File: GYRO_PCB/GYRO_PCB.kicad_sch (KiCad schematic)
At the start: 0 parts

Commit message: feat: add symbols and footprints for principal components
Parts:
- added J1: Pmod GYRO, Connector_PinSocket_2.54mm:PinSocket_2x04_P2.54mm_Vertical, symbol Connector_Generic:Conn_02x04_Counter_Clockwise
- added J2: FLASH Socket 1, Connector_PinSocket_2.54mm:PinSocket_1x08_P2.54mm_Vertical, symbol Connector:Conn_01x08_Socket
- added J3: FLASH Socket 2, Connector_PinSocket_2.54mm:PinSocket_1x08_P2.54mm_Vertical, symbol Connector:Conn_01x08_Socket
- added U1: NUCLEO-F446RE, FOOTPRINTS:NUCLEO-F446RE, symbol NUCLEO-F446RE:NUCLEO-F446RE
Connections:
- new net: U1.CN7_19 (CN7_GND), U1.CN7_20 (CN7_GND), U1.CN7_22 (CN7_GND), U1.CN7_8 (CN7_GND)

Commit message: feat: most of schematic done
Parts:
- removed U1: NUCLEO-F446RE, FOOTPRINTS:NUCLEO-F446RE, symbol NUCLEO-F446RE:NUCLEO-F446RE
- added C1: 0.1uF, symbol Device:C
- added R1, R2, R3: 100k, symbol Device:R
- added R4, R5, R6, R7: 10k, symbol Device:R
- added U1: NUCLEO64-F446RE, FOOTPRINTS:NUCLEO-F446RE, symbol NUCLEO-F446RE:NUCLEO64-F411RE
- J1: footprint Connector_PinSocket_2.54mm:PinSocket_2x04_P2.54mm_Vertical -> GYRO:PinSocket_2x04_P2.54mm_Vertical_Custom
- J3: footprint Connector_PinSocket_2.54mm:PinSocket_1x08_P2.54mm_Vertical -> GYRO:PinSocket_1x08_P2.54mm_Vertical_Custom
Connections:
- net GND: now reaches J3.10 (VSS)
- net GND: now also J1.7 (GND), C1.2
- net NUCLEO_FLASH_SPI2_MOSI: now reaches J3.15 (DQ0)
- net NUCLEO_FLASH_SPI2_MOSI: now also R7.2, U1.CN10_26 (PB15)
- net NUCLEO_FLASH_SCLK: now reaches J3.16 (C)
- net NUCLEO_FLASH_SCLK: now also R6.2, U1.CN5_2 (PC7)
- net at J3.9 (W#/DQ2): now also R3.1
- net at J2.1 (DQ3/HOLD#): now also R1.2
- net +3V3: now reaches J2.2 (VCC)
- net +3V3: now also J1.8 (VCC), C1.1, R1.1, R2.1, R3.2, R4.2, R5.2, R6.1, R7.1
- net at J2.3 (RESET#): now also R2.2
- net NUCLEO_FLASH_CS: now reaches J2.7 (S#)
- net NUCLEO_FLASH_CS: now also R4.1, U1.CN8_3 (PA4)
- net NUCLEO_FLASH_SPI2_MISO: now reaches J2.8 (DQ1)
- net NUCLEO_FLASH_SPI2_MISO: now also R5.1, U1.CN10_28 (PB14)
- net NUCLEO_GYRO_I2C1_SCL: now reaches J1.5 (SCL)
- net NUCLEO_GYRO_I2C1_SCL: now also U1.CN5_10 (PB8)
- net NUCLEO_GYRO_I2C1_SDA: now reaches J1.6 (SDA)
- net NUCLEO_GYRO_I2C1_SDA: now also U1.CN5_9 (PB9)
- no-connect marks 0 -> 11

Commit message: feat: finish PCB draft
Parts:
- added H1, H2, H3, H4: MountingHole, MountingHole:MountingHole_2.2mm_M2_ISO14580, symbol Mechanical:MountingHole
- added J4: Power Terminal, TerminalBlock_MetzConnect:TerminalBlock_MetzConnect_Type011_RT05503HBLC_1x03_P5.00mm_Horizontal, symbol Connector:Screw_Terminal_01x03
- C1: footprint (none) -> Capacitor_THT:C_Disc_D8.0mm_W2.5mm_P5.00mm
- R1, R2, R3, R4, R5, R6, R7: footprint (none) -> Resistor_THT:R_Axial_DIN0207_L6.3mm_D2.5mm_P10.16mm_Horizontal
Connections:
- net +3V3: now also J4.1 (Pin_1)
- net GND: now also U1.CN6_6 (GND), U1.CN6_7 (GND), J4.3 (Pin_3)
- new net NUCLEO_E5V: J4.2 (Pin_2), U1.CN7_6 (E5V)
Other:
- note added: "IMPORTANT: E5V is the external power supply If this order is not respected, the board / PC might be damaged 1. Connect the jumper between pin 2 and pin 3 of JP5 2. Check that JP1 is removed 3. Connect the external power source to E5V (CN7 pin 6) - Already handled by the PCB Use the Power Terminal 4. Power on the external power supply (5 V) 5. Check that LD3 is turned ON 6. Connect the PC to USB c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"
- moved on the sheet: C1, J1, J2, J3, R1, R2, R3, R4, R5, R6, R7

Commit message: Add files via upload
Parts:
- removed J4: Power Terminal, TerminalBlock_MetzConnect:TerminalBlock_MetzConnect_Type011_RT05503HBLC_1x03_P5.00mm_Horizontal, symbol Connector:Screw_Terminal_01x03
- added C2: 0.33uF, Capacitor_THT:C_Disc_D8.0mm_W2.5mm_P5.00mm, symbol Device:C
- added C3: 0.1uF, Capacitor_THT:C_Disc_D8.0mm_W2.5mm_P5.00mm, symbol Device:C
- added J5: Power Terminal - Raw, symbol Connector:Screw_Terminal_01x02
- added U2: uA7805, symbol Regulator_Linear:uA7805
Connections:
- net +3V3: now also U1. (PB13)
- net GND: now also C2.1, C3.1, J5.2 (Pin_2), U2.2 (GND)
- net NUCLEO_E5V: now also C3.2, U2.3 (OUT)
- new net BAT: C2.2, J5.1 (Pin_1), U2.1 (IN)
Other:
- note added: "IMPORTANT: E5V is the external power supply If this order is not respected, the board / PC might be damaged 1. Connect the jumper between pin 2 and pin 3 of JP5 2. Check that JP1 is removed 3. Connect the external power source to E5V (CN7 pin 6) - Already handled by the PCB Use the Power Terminal 4. Power on the external power supply () 5. Check that LD3 is turned ON 6. Connect the PC to USB conn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"
- note removed: "IMPORTANT: E5V is the external power supply If this order is not respected, the board / PC might be damaged 1. Connect the jumper between pin 2 and pin 3 of JP5 2. Check that JP1 is removed 3. Connect the external power source to E5V (CN7 pin 6) - Already handled by the PCB Use the Power Terminal 4. Power on the external power supply (5 V) 5. Check that LD3 is turned ON 6. Connect the PC to USB c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"

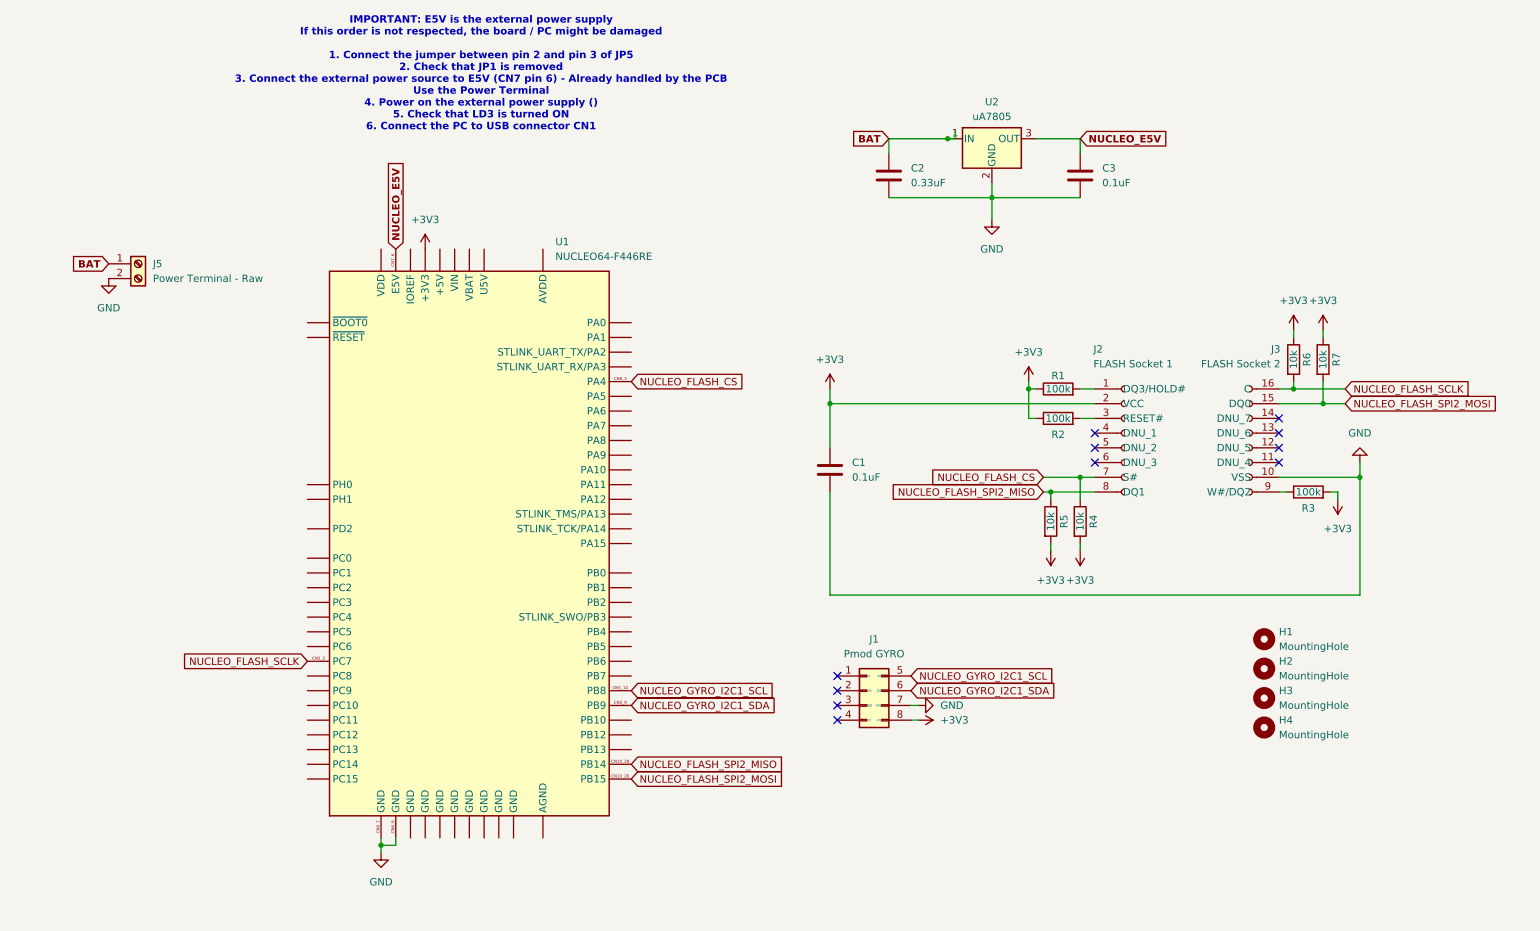
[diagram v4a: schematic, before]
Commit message: New schematic
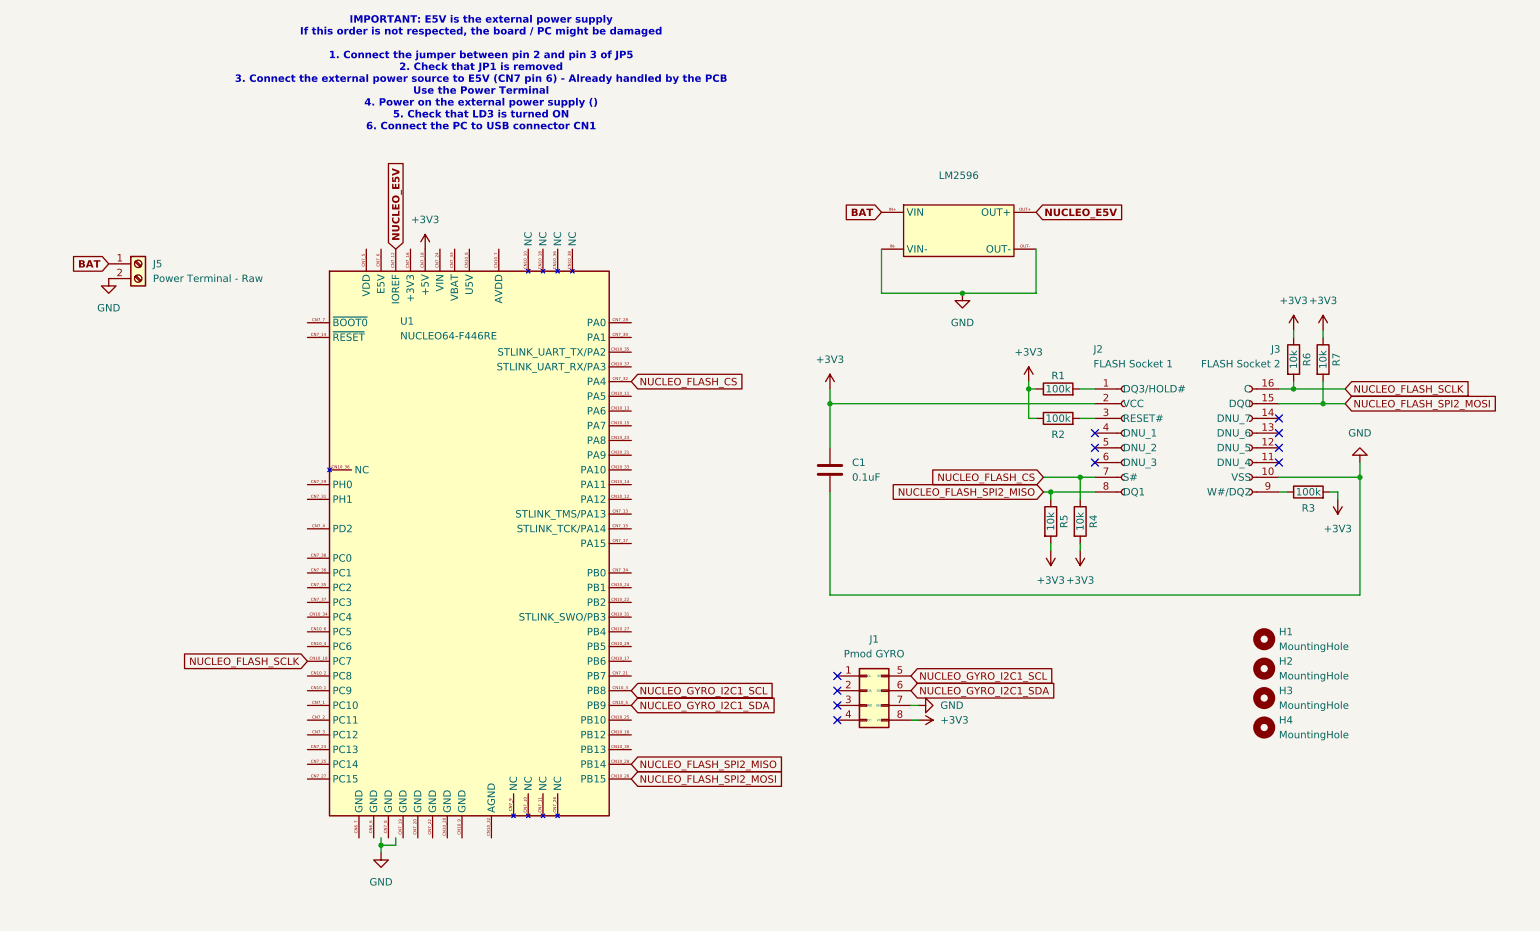
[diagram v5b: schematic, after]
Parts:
- removed C2: 0.33uF, Capacitor_THT:C_Disc_D8.0mm_W2.5mm_P5.00mm, symbol Device:C
- removed C3: 0.1uF, Capacitor_THT:C_Disc_D8.0mm_W2.5mm_P5.00mm, symbol Device:C
- removed U2: uA7805, symbol Regulator_Linear:uA7805
- added LM2596: ~, FOOTPRINTS:LM2596 Module, symbol LM2596_Module:LM2596_Mod
- J5: footprint (none) -> TerminalBlock:TerminalBlock_MaiXu_MX126-5.0-02P_1x02_P5.00mm
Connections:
- net +3V3: now also U1.CN7_18 (+5V); no longer U1. (PB13)
- net BAT: now also LM2596.IN+ (VIN)
- net GND: now also LM2596.IN- (VIN-), LM2596.OUT-; no longer U1.CN6_6 (GND), U1.CN6_7 (GND)
- net NUCLEO_E5V: now also U1.CN7_12 (IOREF), LM2596.OUT+; no longer U1.CN7_6 (E5V)
- net NUCLEO_FLASH_CS: now also U1.CN7_32 (PA4); no longer U1.CN8_3 (PA4)
- net NUCLEO_FLASH_SCLK: now also U1.CN10_19 (PC7); no longer U1.CN5_2 (PC7)
- net NUCLEO_GYRO_I2C1_SCL: now also U1.CN10_3 (PB8); no longer U1.CN5_10 (PB8)
- net NUCLEO_GYRO_I2C1_SDA: now also U1.CN10_5 (PB9); no longer U1.CN5_9 (PB9)

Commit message: new pcb and schematic
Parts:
- removed H1, H2, H3, H4: MountingHole, MountingHole:MountingHole_2.2mm_M2_ISO14580, symbol Mechanical:MountingHole
- added D1: SFH4346, LED_THT:LED_D3.0mm_IRBlack, symbol LED:SFH4346
- added J4: Switch Bat, TerminalBlock:TerminalBlock_MaiXu_MX126-5.0-02P_1x02_P5.00mm, symbol Connector:Screw_Terminal_01x02
- added R8: 330, Resistor_THT:R_Axial_DIN0207_L6.3mm_D2.5mm_P10.16mm_Horizontal, symbol Device:R
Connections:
- net +3V3: now also U1.CN7_16 (+3V3); no longer U1.CN7_18 (+5V)
- net BAT: now also J4.1 (Pin_1); no longer J5.1 (Pin_1)
- net GND: now also D1.1 (K)
- net NUCLEO_E5V: now also U1.CN7_6 (E5V); no longer U1.CN7_12 (IOREF)
- net LED: now reaches U1.CN7_17 (PA15)
- net LED: now also R8.1
- new net: D1.2 (A), R8.2
- new net: J4.2 (Pin_2), J5.1 (Pin_1)
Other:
- note added: "IMPORTANT: E5V is the external power supply If this order is not respected, the board / PC might be damaged 1. Connect the jumper between pin 2 and pin 3 of JP5 2. Check that JP1 is removed 3. Connect the external power source to E5V (CN7 pin 6) - Already handled by the PCB Use the Power Terminal 4. Power on the external power supply (7.4V, 2 Li-Ion batteries) 5. Check that LD3 is turned ON 6. Co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"
- note removed: "IMPORTANT: E5V is the external power supply If this order is not respected, the board / PC might be damaged 1. Connect the jumper between pin 2 and pin 3 of JP5 2. Check that JP1 is removed 3. Connect the external power source to E5V (CN7 pin 6) - Already handled by the PCB Use the Power Terminal 4. Power on the external power supply () 5. Check that LD3 is turned ON 6. Connect the PC to USB conn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"
- moved on the sheet: J5

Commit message: updated footprint for LED
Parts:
- D1: footprint LED_THT:LED_D3.0mm_IRBlack -> LED_THT:LED_D5.0mm_IRBlack
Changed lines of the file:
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@@
 			)
 		)
-		(property "Footprint" "LED_THT:LED_D3.0mm_IRBlack"
+		(property "Footprint" "LED_THT:LED_D5.0mm_IRBlack"
 			(at 238.76 60.325 0)
 			(effects

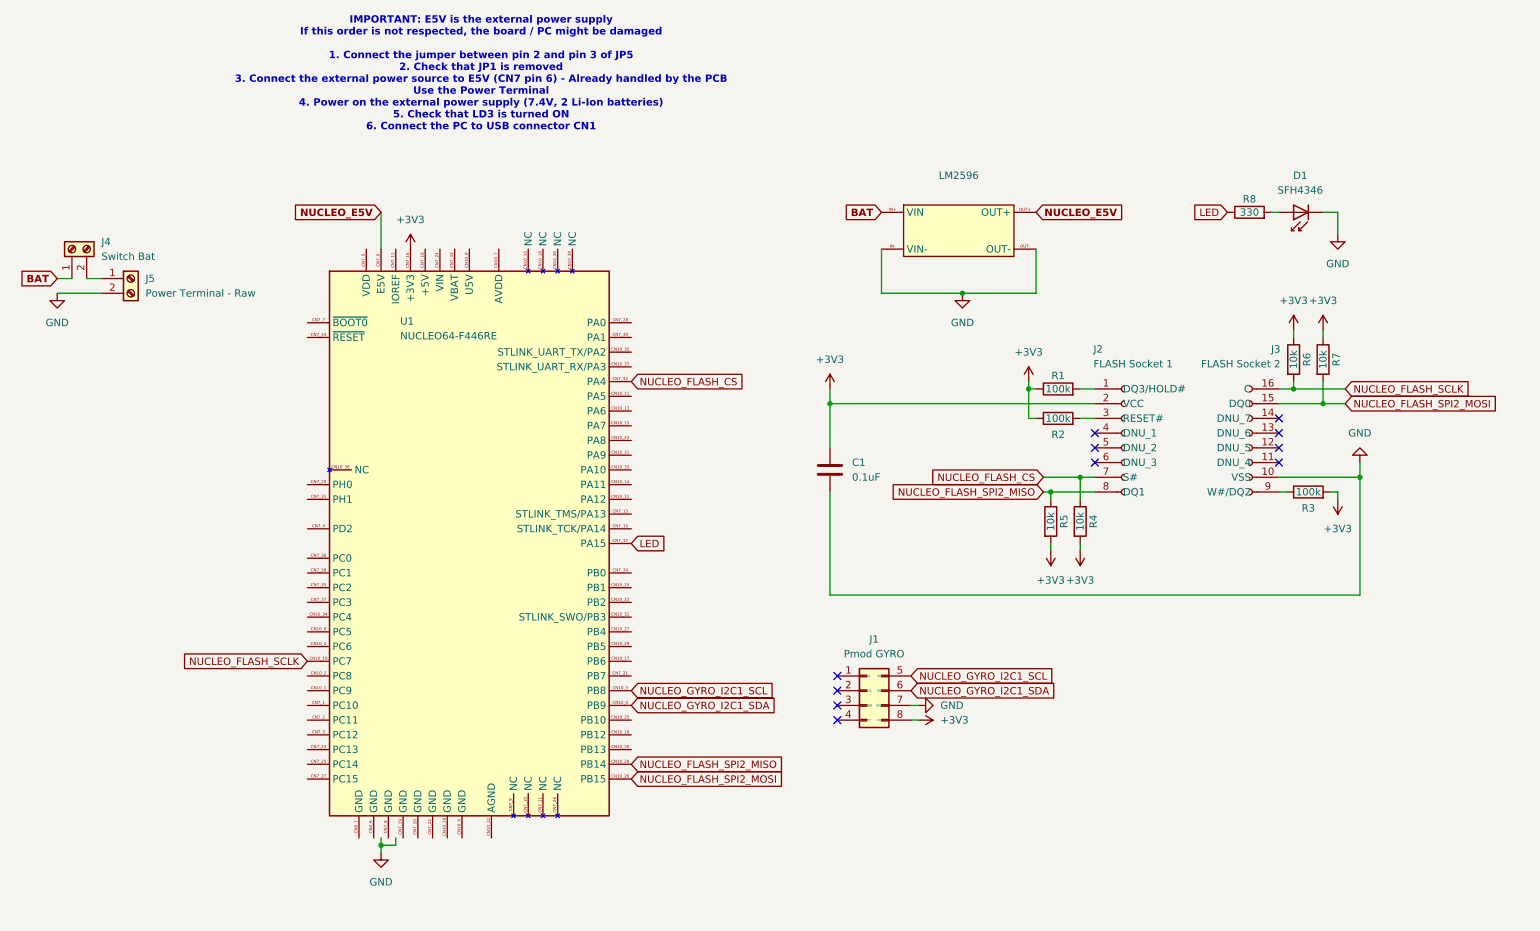
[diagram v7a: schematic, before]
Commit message: refactor: clean schematic & PCB + feat: add LM2596 & terminal 3D models
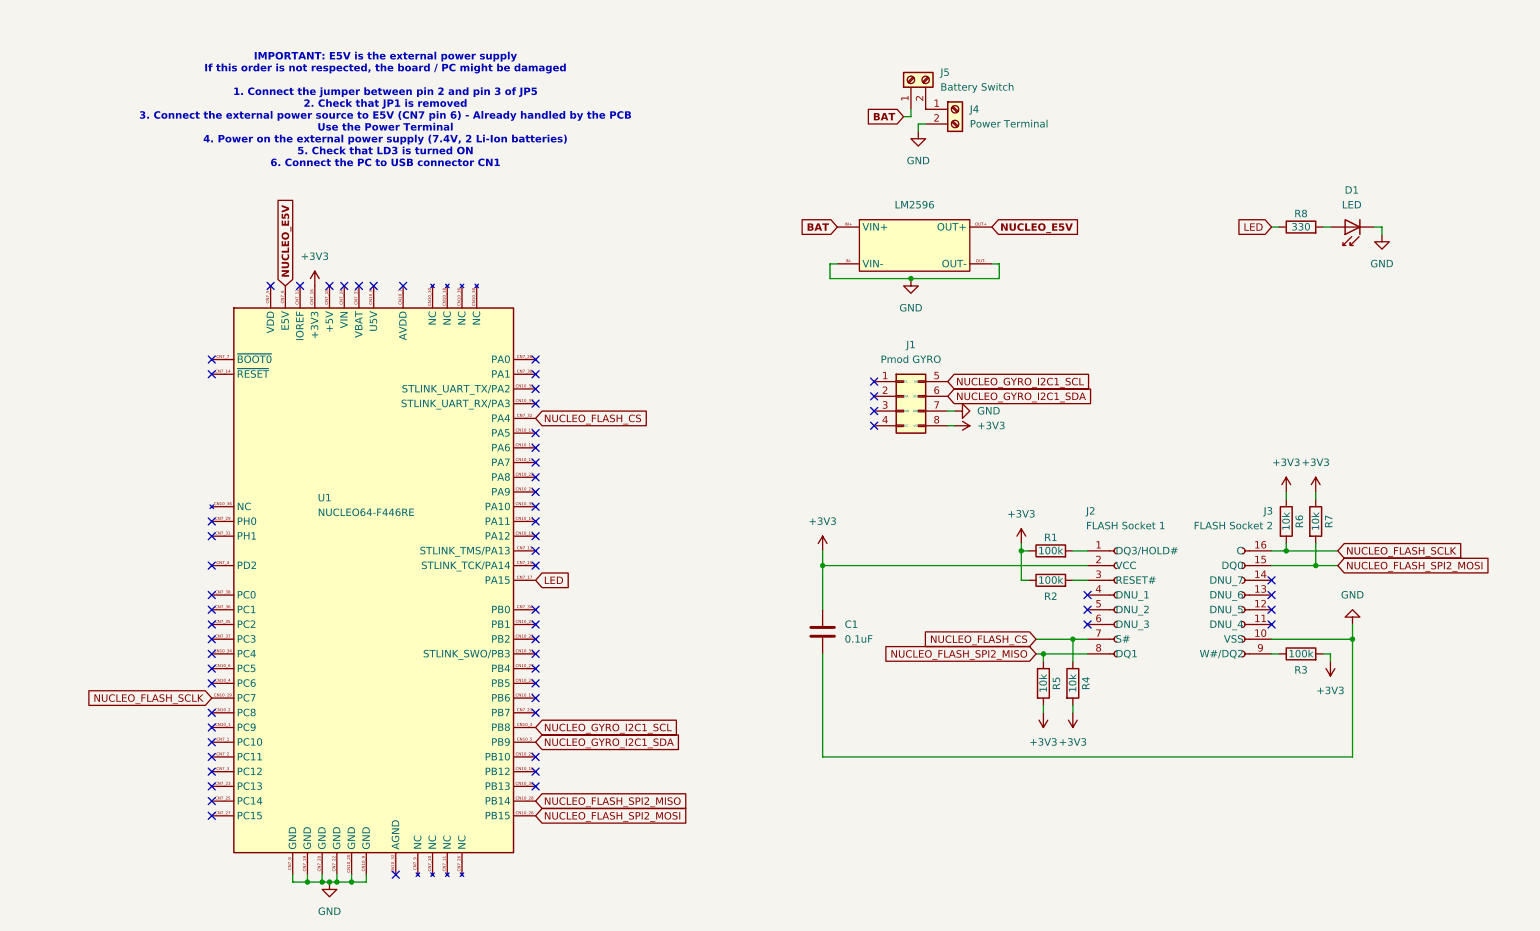
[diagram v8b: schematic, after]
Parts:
- D1: value SFH4346 -> LED
- J4: renamed from J5; value Power Terminal - Raw -> Power Terminal
- J5: renamed from J4; value Switch Bat -> Battery Switch
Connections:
- net GND: now also U1.CN10_20 (GND), U1.CN10_9 (GND), U1.CN7_19 (GND), U1.CN7_20 (GND), U1.CN7_22 (GND), U1.CN7_8 (GND)
- no-connect marks 11 -> 64
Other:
- moved on the sheet: C1, D1, J1, J2, J3, J4, J5, LM2596, R1, R2, R3, R4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
